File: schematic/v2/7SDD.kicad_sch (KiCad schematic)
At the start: 6 parts, among them U18 HDSP-7503, U19 HDSP-7503, U2 HDSP-7503, U4 YAAJ_BluePill_Part_Like

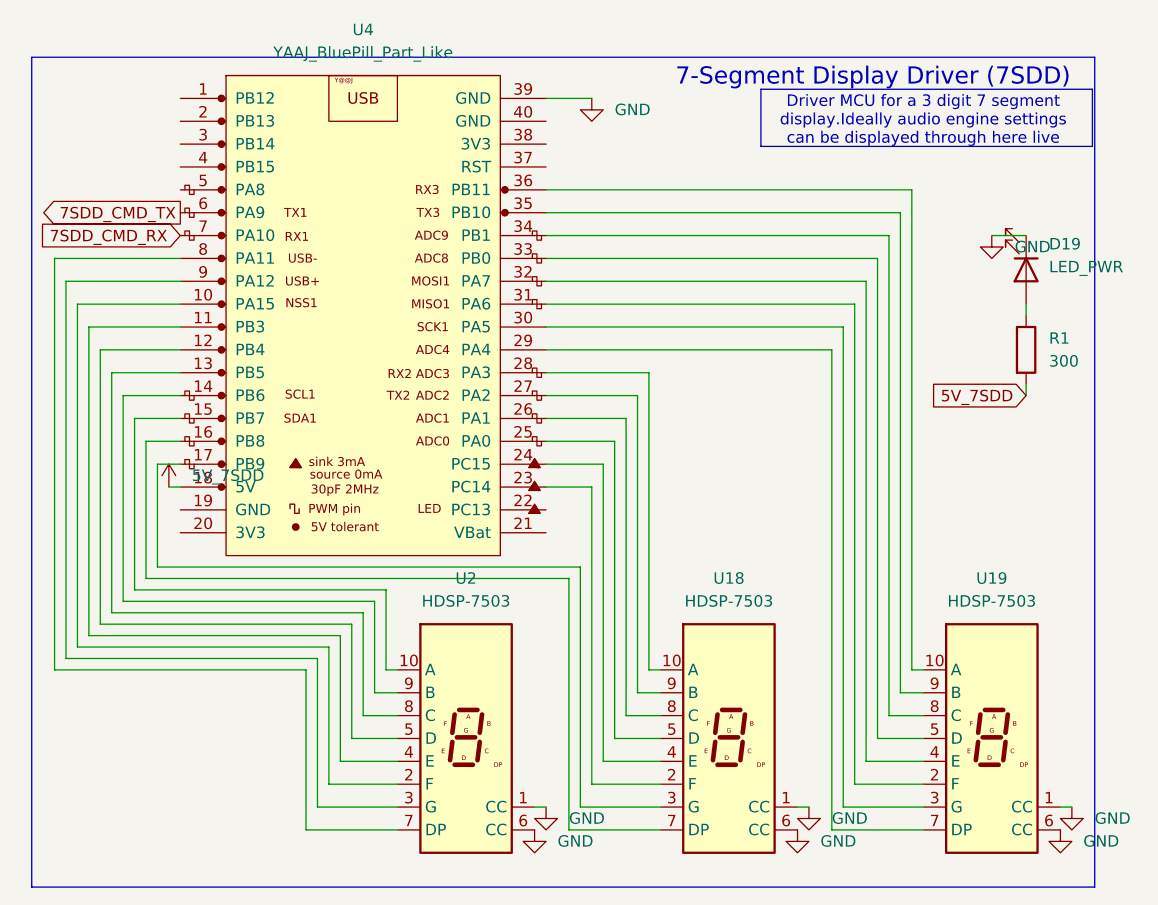
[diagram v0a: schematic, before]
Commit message: progress on putting things in different sheets
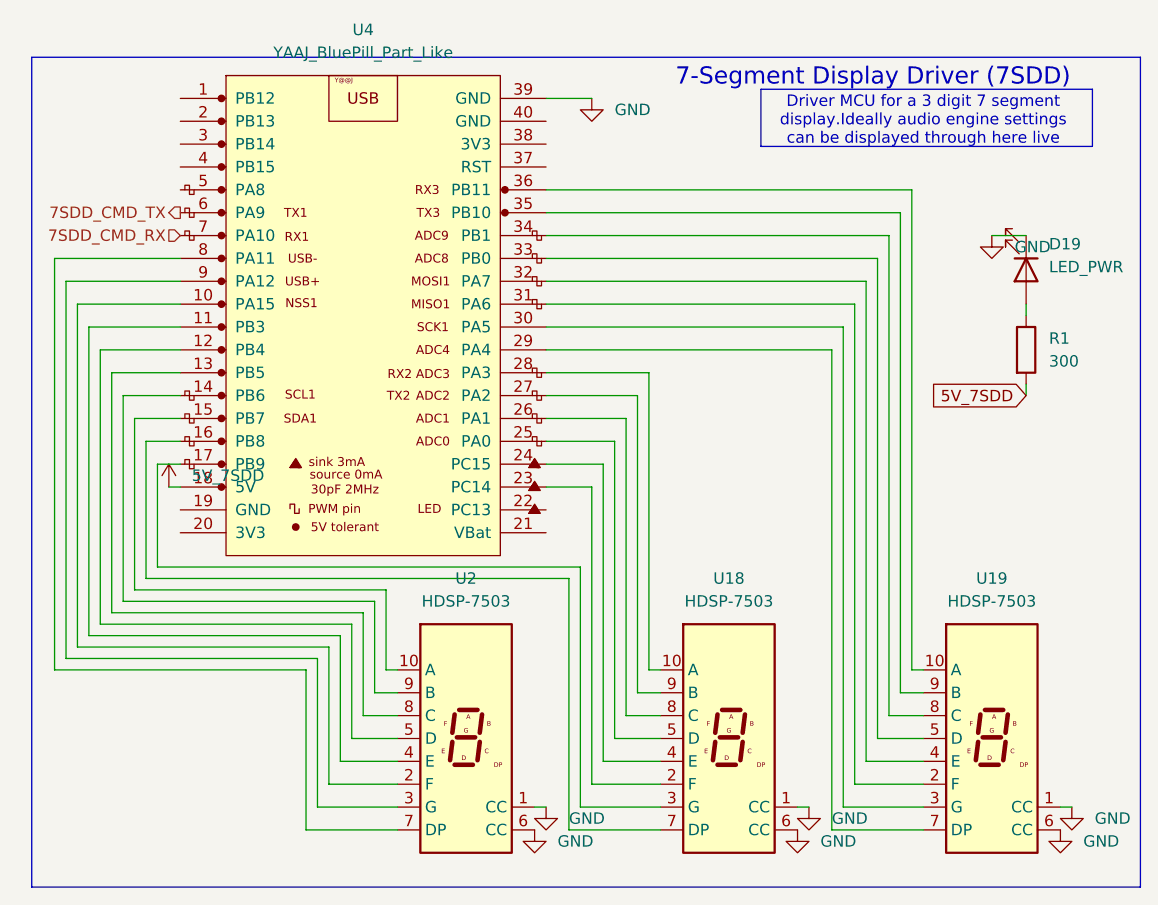
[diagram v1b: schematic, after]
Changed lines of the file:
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@@
 	(rectangle
 		(start 87.63 55.118)
-		(end 205.74 147.32)
+		(end 210.82 147.32)
 		(stroke
 			(width 0)
@@
 			(width 0)
 			(type default)
-		)
-	)
-	(global_label "7SDD_CMD_TX"
-		(shape output)
-		(at 104.14 72.39 180)
-		(fields_autoplaced yes)
-		(effects
-			(font
-				(size 1.27 1.27)
-			)
-			(justify right)
-		)
-		(property "Intersheetrefs" "${INTERSHEET_REFS}"
-			(at 88.0921 72.39 0)
-			(effects
-				(font
-					(size 1.27 1.27)
-				)
-				(justify right)
-				(hide yes)
-			)
 		)
 	)
@@
 		)
 	)
-	(global_label "7SDD_CMD_RX"
+	(hierarchical_label "7SDD_CMD_RX"
 		(shape input)
 		(at 104.14 74.93 180)
-		(fields_autoplaced yes)
 		(effects
 			(font
@@
 			(justify right)
 		)
-		(property "Intersheetrefs" "${INTERSHEET_REFS}"
-			(at 87.7897 74.93 0)
-			(effects
-				(font
-					(size 1.27 1.27)
-				)
-				(justify right)
-				(hide yes)
+	)
+	(hierarchical_label "7SDD_CMD_TX"
+		(shape output)
+		(at 104.14 72.39 180)
+		(effects
+			(font
+				(size 1.27 1.27)
 			)
-		)
-	)
+			(justify right)
+		)
+	)

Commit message: no errors in the ERC!
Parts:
- removed U18, U19, U2: HDSP-7503, Display_7Segment:HDSP-A151, symbol Display_Character:HDSP-7503
- added U18, U2, U36: SM420561N, Display_7Segment:7SegmentLED_LTS6760_LTS6780, symbol Display_Character:SM420561N
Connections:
- net GND: now also U18.3 (CC), U18.8 (CC), U2.3 (CC), U2.8 (CC), U36.3 (CC), U36.8 (CC)
- net at U4.36 (PB11): now also U18.7 (A)
- net at U4.31 (PA6): now also U18.9 (F)
- net at U4.30 (PA5): now also U18.10 (G)
- net at U4.32 (PA7): now also U18.1 (E)
- net at U4.33 (PB0): now also U18.2 (D)
- net at U4.29 (PA4): now also U18.5 (DP)
- net at U4.34 (PB1): now also U18.4 (C)
- net at U4.35 (PB10): now also U18.6 (B)
- net at U4.28 (PA3): now also U2.7 (A)
- net at U4.23 (PC14): now also U2.9 (F)
- net at U4.17 (PB9): now also U2.10 (G)
- net at U4.24 (PC15): now also U2.1 (E)
- net at U4.25 (PA0): now also U2.2 (D)
- net at U4.16 (PB8): now also U2.5 (DP)
- net at U4.26 (PA1): now also U2.4 (C)
- net at U4.27 (PA2): now also U2.6 (B)
- net at U4.15 (PB7): now also U36.7 (A)
- net at U4.10 (PA15): now also U36.9 (F)
- net at U4.9 (PA12): now also U36.10 (G)
- net at U4.11 (PB3): now also U36.1 (E)
- net at U4.12 (PB4): now also U36.2 (D)
- net at U4.8 (PA11): now also U36.5 (DP)
- net at U4.13 (PB5): now also U36.4 (C)
- net at U4.14 (PB6): now also U36.6 (B)
- no-connect marks 0 -> 12

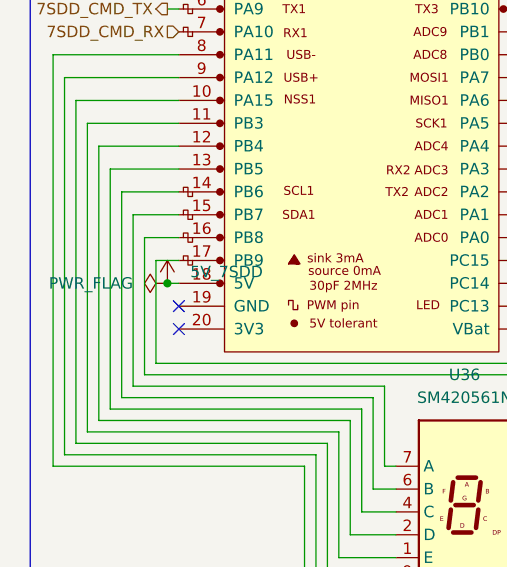
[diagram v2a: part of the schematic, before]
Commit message: schematic updates, no errors at least. running DRC on pcb
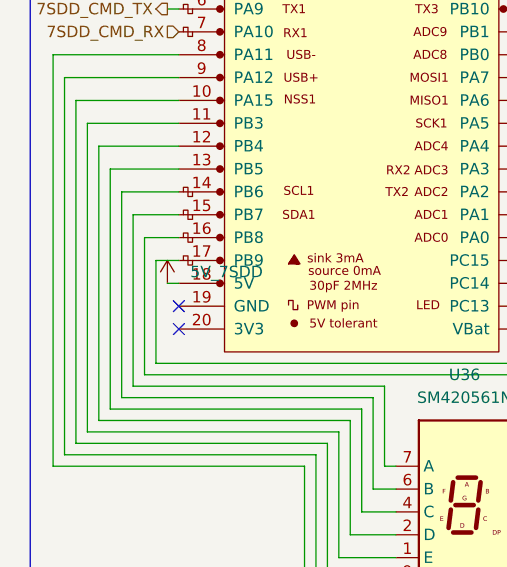
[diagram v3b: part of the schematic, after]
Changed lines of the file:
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@@
 		)
-	)
-	(junction
-		(at 102.87 102.87)
-		(diameter 0)
-		(color 0 0 0 0)
 	)
 	(no_connect
@@
 					(unit 1)
 				)
-			)
-		)
-	)
-	(symbol
-		(lib_id "power:PWR_FLAG")
-		(at 102.87 102.87 90)
-		(unit 1)
-		(exclude_from_sim no)
-		(in_bom yes)
-		(on_board yes)
-		(dnp no)
-		(fields_autoplaced yes)
-		(property "Reference" "#FLG08"
-			(at 100.965 102.87 0)
-			(effects
-				(font
-					(size 1.27 1.27)
-				)
-				(hide yes)
-			)
-		)
-		(property "Value" "PWR_FLAG"
-			(at 99.06 102.8699 90)
-			(effects
-				(font
-					(size 1.27 1.27)
-				)
-				(justify left)
-			)
-		)
-		(property "Footprint" ""
-			(at 102.87 102.87 0)
-			(effects
-				(font
-					(size 1.27 1.27)
-				)
-				(hide yes)
-			)
-		)
-		(property "Datasheet" "~"
-			(at 102.87 102.87 0)
-			(effects
-				(font
-					(size 1.27 1.27)
-				)
-				(hide yes)
-			)
-		)
-		(property "Description" "Special symbol for telling ERC where power comes from"
-			(at 102.87 102.87 0)
-			(effects
-				(font
-					(size 1.27 1.27)
-				)
-				(hide yes)
-			)
-		)
-		(pin "1"
-		)
-		(instances
-			(project ""
-				(path "/fe7b15e9-f0ed-4338-9f03-dd7651dace13/0125ec8c-bf97-4530-be23-1f3b075b267b/03344240-0515-4f71-8710-40bd9ead88e4"
-					(reference "#FLG08")
-					(unit 1)
-				)
